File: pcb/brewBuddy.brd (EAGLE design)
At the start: 89 x 96.7 mm, 3 parts

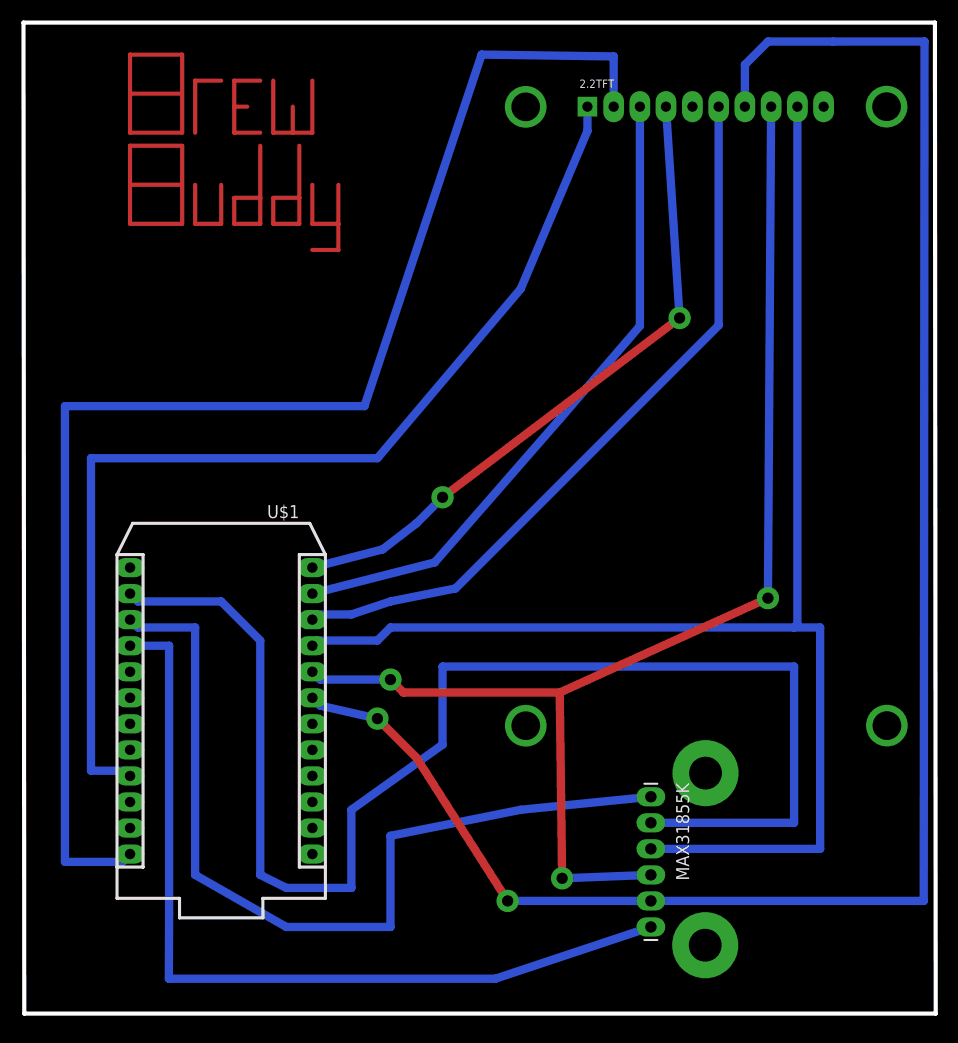
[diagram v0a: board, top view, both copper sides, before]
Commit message: added enclosure files
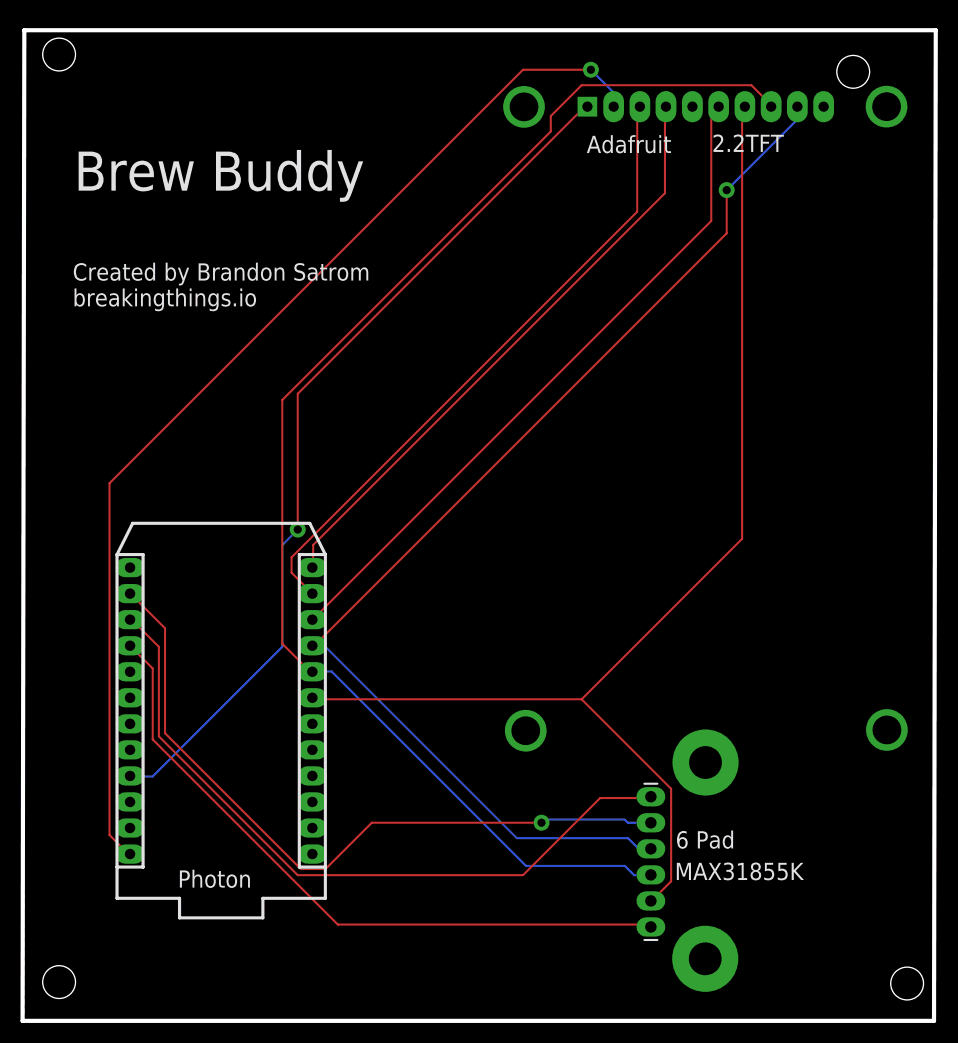
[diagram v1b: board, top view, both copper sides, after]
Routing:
- net N$2: track 136.3 -> 70.0 mm, vias 0 -> 1
- net N$6: track 175.7 -> 115.0 mm, vias 2 -> 0
- net N$7: track 30.5 -> 0.00 mm
- net N$16: track 30.5 -> 0.00 mm
- net N$12: track 135.0 -> 105.2 mm, vias 0 -> 1
- net N$4: track 139.3 -> 113.8 mm, vias 0 -> 1
- net N$13: track 103.2 -> 85.3 mm, vias 0 -> 1
- net N$3: track 84.1 -> 66.3 mm
- net N$15: track 16.5 -> 0.00 mm
- net N$1: track 85.8 -> 69.4 mm
- net N$18: track 15.2 -> 0.00 mm
- net N$19: track 15.2 -> 0.00 mm
- net N$20: track 15.2 -> 0.00 mm
- net N$14: track 11.4 -> 0.00 mm
- net N$17: track 10.2 -> 0.00 mm
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- added copper zone on layer 16, net GND
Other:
- board size 89 x 96.7 mm -> 89.1 x 96.6 mm
- board text added: "Adafruit"
- board text added: "Brew Buddy"
- board text added: "Created by Brandon Satrom breakingthings.io"
- board text added: "Photon"
- board text added: "breakingthings.io"

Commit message: modified sketch to show image on startup; tweaked pcb
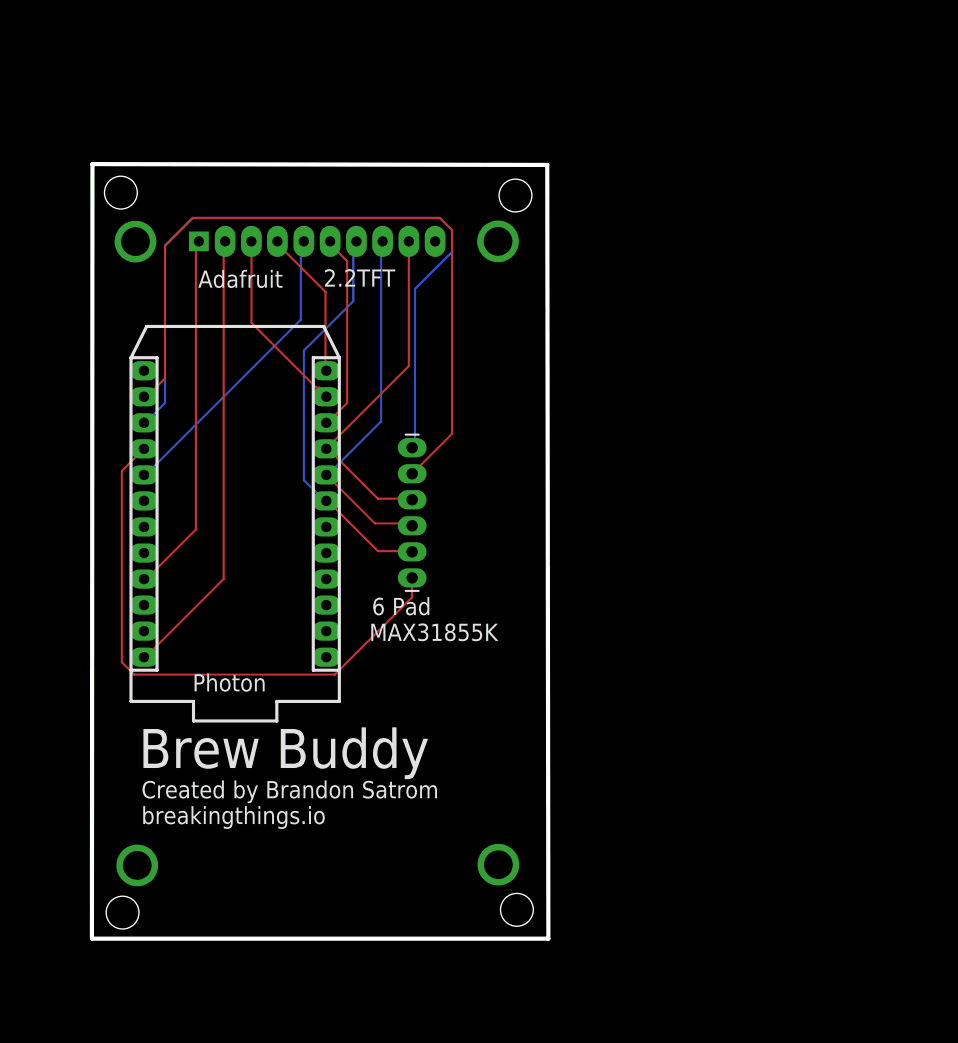
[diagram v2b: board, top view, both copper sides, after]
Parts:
- moved MAX31855K 41.2 mm to (31.3, 48.0)
- moved 2.2TFT 40.1 mm to (20.5, 68.1)
- moved U$1 19.3 mm to (24.2, 59.8)
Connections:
- new net N$7: 2.2TFT.5, U$1.17
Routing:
- net N$5: track 131.3 -> 35.7 mm
- net N$4: track 113.8 -> 34.0 mm, vias 1 -> 0
- net N$6: track 115.0 -> 39.0 mm
- net N$12: track 105.2 -> 43.9 mm, vias 1 -> 0
- net N$13: track 85.3 -> 35.4 mm, vias 1 -> 0
- net N$9: track 66.5 -> 19.4 mm
- net N$10: track 59.3 -> 14.7 mm
- net N$11: track 62.6 -> 18.3 mm
- net N$7: track 0.00 -> 29.4 mm
- net N$3: track 66.3 -> 55.5 mm
- net N$1: track 69.4 -> 70.7 mm
- net N$2: track 70.0 -> 70.7 mm, vias 1 -> 0
- removed copper zone on layer 16, net GND
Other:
- board size 89.1 x 96.6 mm -> 44.5 x 75.6 mm
